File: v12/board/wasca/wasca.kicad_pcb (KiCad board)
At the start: 2 copper layers, 78 parts, among them CN1 CARTRIDGE_EDGE_CONNECTOR, P84 CONN_01X02, U1 74ALVC164245, U11 74ALVC164245, U2 74ALVC164245, U3 74ALVC164245, U4 74ALVC164245, U5 LD1117S33CTR, U8 10M08SCE144I7G, U9 SDRAM_MT48_x16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

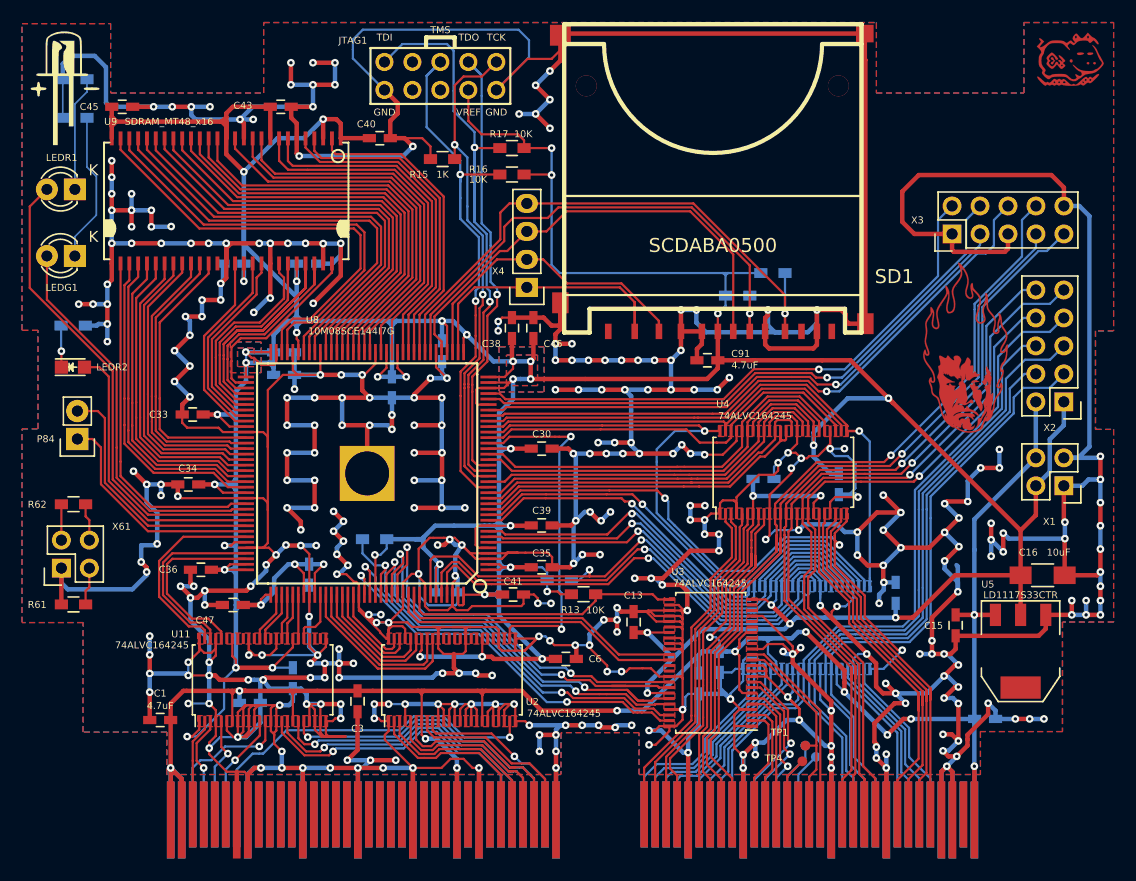
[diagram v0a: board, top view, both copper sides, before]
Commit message: PCB update, added firmware stub
Added USB mezzanine board
Fixed SCSPCLK wiring
Minor changes in cartridge routing
Added MAX10 firmware stub
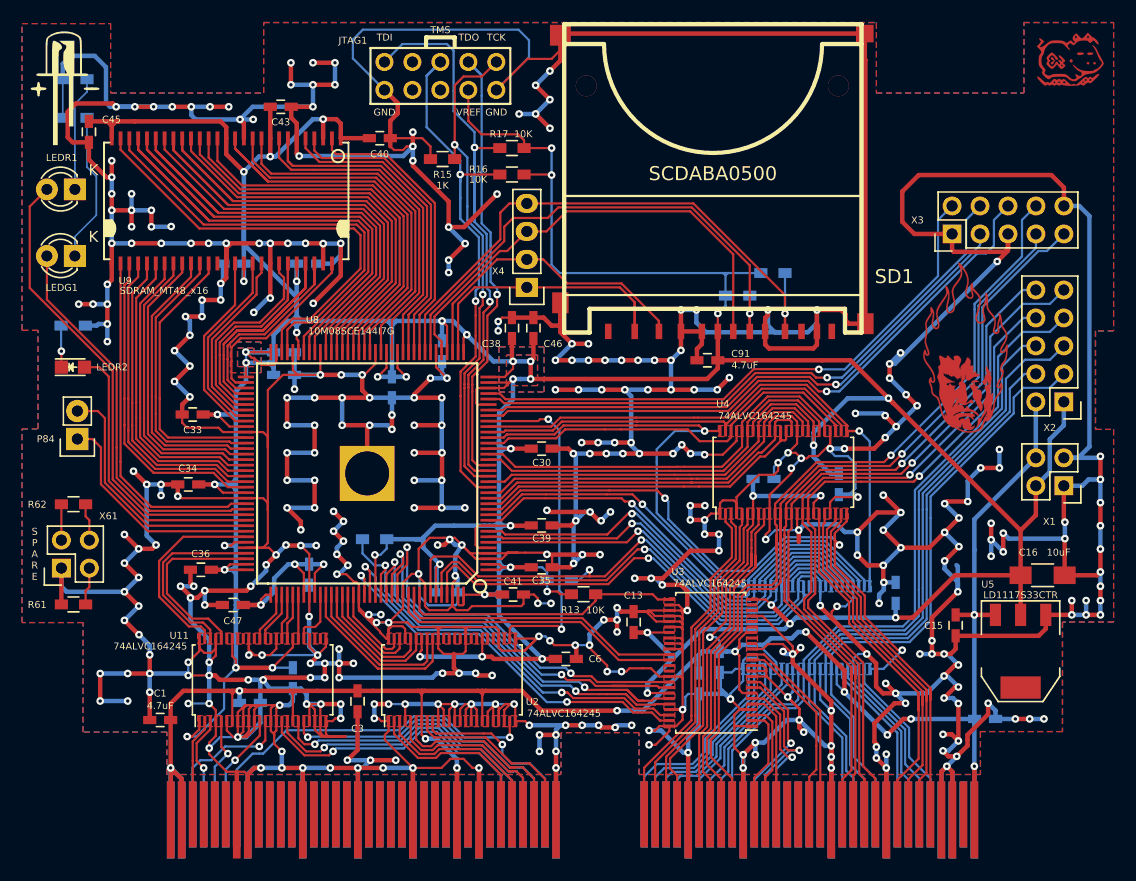
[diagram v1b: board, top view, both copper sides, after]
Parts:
- removed TP1, TP2, TP3, TP4: CONN_01X01, wasca:TEST_PAD
- moved C45 3.79 mm to (33.4, 91.3), turned to 270 degrees
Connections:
- CN1 pad A50: /ABUS_FC0 -> (no net)
- CN1 pad A51: /ABUS_TIM0 -> (no net)
- CN1 pad B50: /ABUS_FC1 -> (no net)
- U8 pad 24: /SCSPCLK_3V -> /ABUS_3V_MUX13
- U8 pad 25: /ABUS_3V_MUX13 -> /ABUS_3V_MUX_EN1
- U8 pad 26: /ABUS_3V_MUX_EN1 -> /ABUS_3V_MUX12
- U8 pad 27: /ABUS_3V_MUX12 -> /ABUS_3V_MUX_EN2
- U8 pad 28: /ABUS_3V_MUX_EN2 -> /SCSPCLK_3V
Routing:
- net GND: track 1650.5 -> 1754.2 mm, vias 360 -> 393
- net /SDR_A1: track 39.7 -> 48.6 mm
- net /SDR_A0: track 39.3 -> 47.7 mm
- net /SDR_A10: track 39.1 -> 46.7 mm
- net /ABUS_FC0: track 6.94 -> 0.00 mm
- net /SDR_BA0: track 38.1 -> 44.7 mm
- net /SDR_CS: track 37.7 -> 43.8 mm
- net /ABUS_TIM0: track 5.89 -> 0.00 mm
- net /ABUS_FC1: track 5.40 -> 0.00 mm
- net /+3_3V: track 588.6 -> 583.4 mm, vias 45 -> 46
- net /ABUS_A0: track 72.9 -> 77.7 mm
- net /SDR_DQ7: track 34.7 -> 38.3 mm
- net /ABUS_A2: track 77.1 -> 79.7 mm
- net /ABUS_CS2: track 14.3 -> 16.2 mm
- net /SDR_DQ4: track 32.0 -> 30.4 mm
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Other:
- board text added: "A2 A0"
- board text added: "D5 A1 D1 D3 3V3"
- board text added: "D6 D4 D0 D2 5V"
- board text added: "GND D7"
- board text added: "Mfg. date : 2016 July 11"
- board text added: "RD CS"
- board text added: "S P A R E"
- board text added: "SP1 GND"
- board text added: "SP2 GND"
- board text added: "X2"
- board text added: "X3"
- board text removed: "Mfg. date : 2016 July 08"
- board text removed: "PCB Order Nb"
- board text removed: "Soldering Date"
